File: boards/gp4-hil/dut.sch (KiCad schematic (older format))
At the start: 0 parts

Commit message: Continued HiL test board
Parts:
- added P?: CONN_01X20, symbol CONN_01X20
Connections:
- new net DUT_GPIO10: P?.10 (P10)
- new net DUT_GPIO12: P?.12 (P12)
- new net DUT_GPIO13: P?.13 (P13)
- new net DUT_GPIO14: P?.14 (P14)
- new net DUT_GPIO15: P?.15 (P15)
- new net DUT_GPIO16: P?.16 (P16)
- new net DUT_GPIO17: P?.17 (P17)
- new net DUT_GPIO18: P?.18 (P18)
- new net DUT_GPIO19: P?.19 (P19)
- new net DUT_GPIO2: P?.2 (P2)
- new net DUT_GPIO20: P?.20 (P20)
- new net DUT_GPIO3: P?.3 (P3)
- new net DUT_GPIO4: P?.4 (P4)
- new net DUT_GPIO5: P?.5 (P5)
- new net DUT_GPIO6: P?.6 (P6)
- new net DUT_GPIO7: P?.7 (P7)
- new net DUT_GPIO8: P?.8 (P8)
- new net DUT_GPIO9: P?.9 (P9)
- new net DUT_VDD1: P?.1 (P1)
- new net GND: P?.11 (P11)
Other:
- note added: "TODO: Buffered indicator LEDs"
- note added: "TODO: Pass transistor to enable DUT_VDD2"
- note added: "Total number of switches needed:\n* 18 GPIO -> FPGA\n* 15 GPIO -> DAC\n* 2 Vdd -> regulator\n\nADC is always connected\n\nNeed >8V compatible switch (in open state) for FPGA->GPIO2"
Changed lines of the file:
@@
 LIBS:special-azonenberg
 LIBS:xilinx-azonenberg
+LIBS:conn
+LIBS:gp4-hil-cache
 EELAYER 25 0
 EELAYER END
 $Descr A4 11693 8268
 encoding utf-8
-Sheet 1 6
+Sheet 5 7
 Title "GreenPak Hardware-In-Loop Test Platform"
 Date "2016-05-09"
@@
 Comment4 ""
 $EndDescr
+$Comp
+L CONN_01X20 P?
+U 1 1 5731797F
+P 1400 1900
+F 0 "P?" H 1478 1938 50  0000 L CNN
+F 1 "CONN_01X20" H 1478 1846 50  0000 L CNN
+F 2 "" H 1400 1900 60  0000 C CNN
+F 3 "" H 1400 1900 60  0000 C CNN
+	1    1400 1900
+	-1   0    0    -1
+$EndComp
+Text HLabel 1900 950  2    60   Input ~ 0
+DUT_VDD1
+Wire Wire Line
+	1900 950  1600 950
+Wire Wire Line
+	1600 1050 2400 1050
+Text HLabel 2400 4850 2    60   Input ~ 0
+DUT_VPP
+Text HLabel 2350 4600 2    60   Input ~ 0
+DUT_VDD2
+Text HLabel 1900 1950 2    60   Input ~ 0
+GND
+Text Notes 2150 4200 0    60   ~ 0
+TODO: Pass transistor to enable DUT_VDD2
+Text Notes 2150 4300 0    60   ~ 0
+TODO: Buffered indicator LEDs
+Text Label 2400 1150 0    60   ~ 0
+DUT_GPIO3
+Wire Wire Line
+	1900 1950 1600 1950
+Text Label 2400 1250 0    60   ~ 0
+DUT_GPIO4
+Text Label 2400 1350 0    60   ~ 0
+DUT_GPIO5
+Text Label 2400 1450 0    60   ~ 0
+DUT_GPIO6
+Text Label 2400 1550 0    60   ~ 0
+DUT_GPIO7
+Text Label 2400 1650 0    60   ~ 0
+DUT_GPIO8
+Text Label 2400 1750 0    60   ~ 0
+DUT_GPIO9
+Text Label 2400 1850 0    60   ~ 0
+DUT_GPIO10
+Text Label 2400 2050 0    60   ~ 0
+DUT_GPIO12
+Text Label 2400 2150 0    60   ~ 0
+DUT_GPIO13
+Text Label 2400 2250 0    60   ~ 0
+DUT_GPIO14
+Text Label 2400 2350 0    60   ~ 0
+DUT_GPIO15
+Text Label 2400 2450 0    60   ~ 0
+DUT_GPIO16
+Text Label 2400 2550 0    60   ~ 0
+DUT_GPIO17
+Text Label 2400 2650 0    60   ~ 0
+DUT_GPIO18
+Text Label 2400 2750 0    60   ~ 0
+DUT_GPIO19
+Text Label 2400 2850 0    60   ~ 0
+DUT_GPIO20
+Wire Wire Line
+	1600 1150 2400 1150
+Wire Wire Line
+	2400 1250 1600 1250
+Wire Wire Line
+	1600 1350 2400 1350
+Wire Wire Line
+	2400 1450 1600 1450
+Wire Wire Line
+	1600 1550 2400 1550
+Wire Wire Line
+	2400 1650 1600 1650
+Wire Wire Line
+	1600 1750 2400 1750
+Wire Wire Line
+	2400 1850 1600 1850
+Wire Wire Line
+	2400 2050 1600 2050
+Wire Wire Line
+	1600 2150 2400 2150
+Wire Wire Line
+	2400 2250 1600 2250
+Wire Wire Line
+	1600 2350 2400 2350
+Wire Wire Line
+	2400 2450 1600 2450
+Wire Wire Line
+	1600 2550 2400 2550
+Wire Wire Line
+	2400 2650 1600 2650
+Wire Wire Line
+	2400 2750 1600 2750
+Wire Wire Line
+	1600 2850 2400 2850
+Text Notes 2150 4000 0    60   ~ 0
+Total number of switches needed:\n* 18 GPIO -> FPGA\n* 15 GPIO -> DAC\n* 2 Vdd -> regulator\n\nADC is always connected\n\nNeed >8V compatible switch (in open state) for FPGA->GPIO2
+Text Label 2400 1050 0    60   ~ 0
+DUT_GPIO2
 $EndSCHEMATC

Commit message: Continued work on gp4-hil board schematic
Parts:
- added U1, U4: TS3A4751, symbol TS3A4751
- gave numbers to parts that had none: 1
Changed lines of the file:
@@
 EELAYER 25 0
 EELAYER END
-$Descr A4 11693 8268
+$Descr A3 16535 11693
 encoding utf-8
 Sheet 5 7
 Title "GreenPak Hardware-In-Loop Test Platform"
-Date "2016-05-09"
+Date "2016-05-10"
 Rev "0.1"
 Comp "Andrew Zonenberg"
@@
 $EndDescr
 $Comp
-L CONN_01X20 P?
+L CONN_01X20 P1
 U 1 1 5731797F
 P 1400 1900
-F 0 "P?" H 1478 1938 50  0000 L CNN
+F 0 "P1" H 1478 1938 50  0000 L CNN
 F 1 "CONN_01X20" H 1478 1846 50  0000 L CNN
 F 2 "" H 1400 1900 60  0000 C CNN
@@
 Text Label 2400 1050 0    60   ~ 0
 DUT_GPIO2
+$Comp
+L TS3A4751 U1
+U 1 1 5732B5B9
+P 1700 6000
+F 0 "U1" H 2300 6050 60  0000 C CNN
+F 1 "TS3A4751" H 1900 5950 60  0000 C CNN
+F 2 "" H 1700 6000 60  0000 C CNN
+F 3 "" H 1700 6000 60  0000 C CNN
+	1    1700 6000
+	1    0    0    -1
+$EndComp
+$Comp
+L TS3A4751 U1
+U 2 1 5732C1D7
+P 1700 6600
+F 0 "U1" H 2300 6650 60  0000 C CNN
+F 1 "TS3A4751" H 1900 6550 60  0000 C CNN
+F 2 "" H 1700 6600 60  0000 C CNN
+F 3 "" H 1700 6600 60  0000 C CNN
+	2    1700 6600
+	1    0    0    -1
+$EndComp
+$Comp
+L TS3A4751 U1
+U 3 1 5732C21D
+P 3200 6000
+F 0 "U1" H 3800 6050 60  0000 C CNN
+F 1 "TS3A4751" H 3400 5950 60  0000 C CNN
+F 2 "" H 3200 6000 60  0000 C CNN
+F 3 "" H 3200 6000 60  0000 C CNN
+	3    3200 6000
+	1    0    0    -1
+$EndComp
+$Comp
+L TS3A4751 U1
+U 4 1 5732C2B5
+P 3200 6600
+F 0 "U1" H 3800 6650 60  0000 C CNN
+F 1 "TS3A4751" H 3400 6550 60  0000 C CNN
+F 2 "" H 3200 6600 60  0000 C CNN
+F 3 "" H 3200 6600 60  0000 C CNN
+	4    3200 6600
+	1    0    0    -1
+$EndComp
+$Comp
+L TS3A4751 U4
+U 4 1 5732C31D
+P 4300 6600
+F 0 "U4" H 4900 6650 60  0000 C CNN
+F 1 "TS3A4751" H 4500 6550 60  0000 C CNN
+F 2 "" H 4300 6600 60  0000 C CNN
+F 3 "" H 4300 6600 60  0000 C CNN
+	4    4300 6600
+	1    0    0    -1
+$EndComp
 $EndSCHEMATC

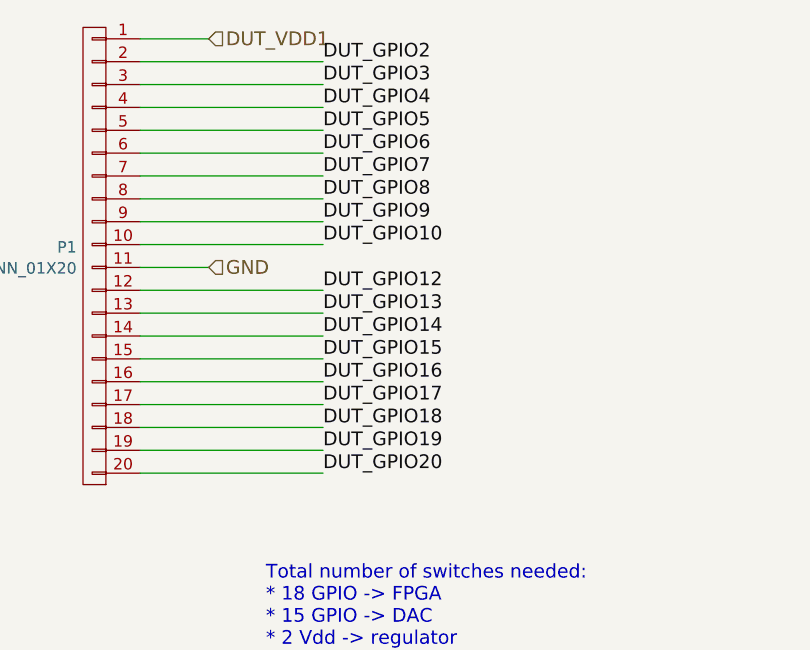
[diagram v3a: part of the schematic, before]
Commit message: Continued analog input schematic
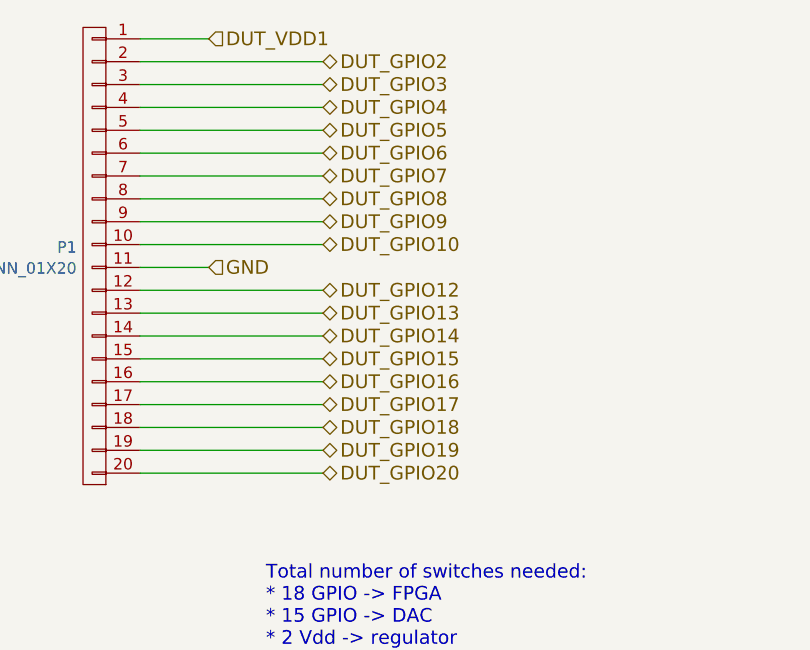
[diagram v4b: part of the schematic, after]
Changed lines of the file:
@@
 Text Notes 2150 4300 0    60   ~ 0
 TODO: Buffered indicator LEDs
-Text Label 2400 1150 0    60   ~ 0
-DUT_GPIO3
 Wire Wire Line
 	1900 1950 1600 1950
-Text Label 2400 1250 0    60   ~ 0
-DUT_GPIO4
-Text Label 2400 1350 0    60   ~ 0
-DUT_GPIO5
-Text Label 2400 1450 0    60   ~ 0
-DUT_GPIO6
-Text Label 2400 1550 0    60   ~ 0
-DUT_GPIO7
-Text Label 2400 1650 0    60   ~ 0
-DUT_GPIO8
-Text Label 2400 1750 0    60   ~ 0
-DUT_GPIO9
-Text Label 2400 1850 0    60   ~ 0
-DUT_GPIO10
-Text Label 2400 2050 0    60   ~ 0
-DUT_GPIO12
-Text Label 2400 2150 0    60   ~ 0
-DUT_GPIO13
-Text Label 2400 2250 0    60   ~ 0
-DUT_GPIO14
-Text Label 2400 2350 0    60   ~ 0
-DUT_GPIO15
-Text Label 2400 2450 0    60   ~ 0
-DUT_GPIO16
-Text Label 2400 2550 0    60   ~ 0
-DUT_GPIO17
-Text Label 2400 2650 0    60   ~ 0
-DUT_GPIO18
-Text Label 2400 2750 0    60   ~ 0
-DUT_GPIO19
-Text Label 2400 2850 0    60   ~ 0
-DUT_GPIO20
 Wire Wire Line
 	1600 1150 2400 1150
@@
 Text Notes 2150 4000 0    60   ~ 0
 Total number of switches needed:\n* 18 GPIO -> FPGA\n* 15 GPIO -> DAC\n* 2 Vdd -> regulator\n\nADC is always connected\n\nNeed >8V compatible switch (in open state) for FPGA->GPIO2
-Text Label 2400 1050 0    60   ~ 0
-DUT_GPIO2
 $Comp
 L TS3A4751 U1
@@
 	1    0    0    -1
 $EndComp
+Text HLabel 2400 1050 2    60   BiDi ~ 0
+DUT_GPIO2
+Text HLabel 2400 1150 2    60   BiDi ~ 0
+DUT_GPIO3
+Text HLabel 2400 1250 2    60   BiDi ~ 0
+DUT_GPIO4
+Text HLabel 2400 1350 2    60   BiDi ~ 0
+DUT_GPIO5
+Text HLabel 2400 1450 2    60   BiDi ~ 0
+DUT_GPIO6
+Text HLabel 2400 1550 2    60   BiDi ~ 0
+DUT_GPIO7
+Text HLabel 2400 1650 2    60   BiDi ~ 0
+DUT_GPIO8
+Text HLabel 2400 1750 2    60   BiDi ~ 0
+DUT_GPIO9
+Text HLabel 2400 1850 2    60   BiDi ~ 0
+DUT_GPIO10
+Text HLabel 2400 2050 2    60   BiDi ~ 0
+DUT_GPIO12
+Text HLabel 2400 2150 2    60   BiDi ~ 0
+DUT_GPIO13
+Text HLabel 2400 2250 2    60   BiDi ~ 0
+DUT_GPIO14
+Text HLabel 2400 2350 2    60   BiDi ~ 0
+DUT_GPIO15
+Text HLabel 2400 2450 2    60   BiDi ~ 0
+DUT_GPIO16
+Text HLabel 2400 2550 2    60   BiDi ~ 0
+DUT_GPIO17
+Text HLabel 2400 2650 2    60   BiDi ~ 0
+DUT_GPIO18
+Text HLabel 2400 2750 2    60   BiDi ~ 0
+DUT_GPIO19
+Text HLabel 2400 2850 2    60   BiDi ~ 0
+DUT_GPIO20
 $EndSCHEMATC

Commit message: Schematic entry for 1V0 PSU
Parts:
- removed U1, U4: TS3A4751, symbol TS3A4751
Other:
- note added: "TODO: Expansion header of some sort\nTODO: Probe clips on every pin"
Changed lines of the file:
@@
 Sheet 5 8
 Title "GreenPak Hardware-In-Loop Test Platform"
-Date "2016-05-14"
+Date "2016-05-15"
 Rev "0.1"
 Comp "Andrew Zonenberg"
@@
 Text HLabel 2400 4850 2    60   Input ~ 0
 DUT_VPP
-Text HLabel 2350 4600 2    60   Input ~ 0
+Text HLabel 2400 4750 2    60   Input ~ 0
 DUT_VDD2
 Text HLabel 1900 1950 2    60   Input ~ 0
@@
 Text Notes 2150 4000 0    60   ~ 0
 Total number of switches needed:\n* 18 GPIO -> FPGA\n* 15 GPIO -> DAC\n* 2 Vdd -> regulator\n\nADC is always connected\n\nNeed >8V compatible switch (in open state) for FPGA->GPIO2
-$Comp
-L TS3A4751 U1
-U 1 1 5732B5B9
-P 1700 6000
-F 0 "U1" H 2300 6050 60  0000 C CNN
-F 1 "TS3A4751" H 1900 5950 60  0000 C CNN
-F 2 "" H 1700 6000 60  0000 C CNN
-F 3 "" H 1700 6000 60  0000 C CNN
-	1    1700 6000
-	1    0    0    -1
-$EndComp
-$Comp
-L TS3A4751 U1
-U 2 1 5732C1D7
-P 1700 6600
-F 0 "U1" H 2300 6650 60  0000 C CNN
-F 1 "TS3A4751" H 1900 6550 60  0000 C CNN
-F 2 "" H 1700 6600 60  0000 C CNN
-F 3 "" H 1700 6600 60  0000 C CNN
-	2    1700 6600
-	1    0    0    -1
-$EndComp
-$Comp
-L TS3A4751 U1
-U 3 1 5732C21D
-P 3200 6000
-F 0 "U1" H 3800 6050 60  0000 C CNN
-F 1 "TS3A4751" H 3400 5950 60  0000 C CNN
-F 2 "" H 3200 6000 60  0000 C CNN
-F 3 "" H 3200 6000 60  0000 C CNN
-	3    3200 6000
-	1    0    0    -1
-$EndComp
-$Comp
-L TS3A4751 U1
-U 4 1 5732C2B5
-P 3200 6600
-F 0 "U1" H 3800 6650 60  0000 C CNN
-F 1 "TS3A4751" H 3400 6550 60  0000 C CNN
-F 2 "" H 3200 6600 60  0000 C CNN
-F 3 "" H 3200 6600 60  0000 C CNN
-	4    3200 6600
-	1    0    0    -1
-$EndComp
-$Comp
-L TS3A4751 U4
-U 4 1 5732C31D
-P 4300 6600
-F 0 "U4" H 4900 6650 60  0000 C CNN
-F 1 "TS3A4751" H 4500 6550 60  0000 C CNN
-F 2 "" H 4300 6600 60  0000 C CNN
-F 3 "" H 4300 6600 60  0000 C CNN
-	4    4300 6600
-	1    0    0    -1
-$EndComp
 Text HLabel 2400 1050 2    60   BiDi ~ 0
 DUT_GPIO2
@@
 Text HLabel 2400 2850 2    60   BiDi ~ 0
 DUT_GPIO20
+Text Notes 6900 3300 0    60   ~ 0
+TODO: Expansion header of some sort\nTODO: Probe clips on every pin
 $EndSCHEMATC
